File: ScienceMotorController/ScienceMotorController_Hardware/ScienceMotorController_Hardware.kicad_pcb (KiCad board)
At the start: 2 copper layers, 124.5 x 120.6 mm, 114 parts, among them SW1 SW_Push, SW2 SW_Push, SW3 SW_Push, SW4 SW_Push, SW5 SW_Push, U1 TM4C129E_Launchpad, U2 3.3V OKI, U4 VNH5019A_E, U5 VNH5019A_E, U6 VNH5019A_E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

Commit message: BOM
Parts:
- SW5: value SW_Push -> SW_SPDT; footprint Button_Switch_SMD:SW_SPST_TL3305A -> Button_Switch_THT:SW_CuK_OS102011MA1QN1_SPDT_Angled
- moved SW5 21.1 mm to (40.9, 116.1), turned to 270 degrees
- moved R56 16.5 mm to (45.5, 113.2), turned to 180 degrees
- moved SW3 5.59 mm to (49.7, 125.2)
- moved R31 5.59 mm to (41.5, 126.7)
- moved R32 5.59 mm to (59.8, 126.7)
- moved SW4 5.59 mm to (67.9, 125.2)
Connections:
- SW5 pad 1: +3V3 -> MSW_5
- SW5 pad 2: MSW_5 -> +3V3
- U1 pad PD3: MSW_5 -> MSW_4
- U1 pad PE0: MSW_1 -> MSW_5
- U1 pad PE1: MSW_2 -> MSW_1
- U1 pad PE3: MSW_4 -> MSW_2
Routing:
- net +3V3: track 473.8 -> 457.9 mm
- net MSW_5: track 19.8 -> 28.6 mm, vias 1 -> 0
- net MSW_4: track 38.8 -> 47.1 mm, vias 1 -> 3
- net MSW_3: track 23.9 -> 18.3 mm
- net MSW_2: track 53.4 -> 48.3 mm
- net MSW_1: track 38.0 -> 34.3 mm

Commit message: PRR Complete
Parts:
- added R34: 0, Resistor_SMD:R_0603_1608Metric_Pad1.05x0.95mm_HandSolder, F.Cu at (50.7, 96.8)
- added R57: 0, Resistor_SMD:R_0603_1608Metric_Pad1.05x0.95mm_HandSolder, F.Cu at (104.6, 96.8)
- added R58: 0, Resistor_SMD:R_0603_1608Metric_Pad1.05x0.95mm_HandSolder, F.Cu at (46.2, 96.8)
- added R59: 0, Resistor_SMD:R_0603_1608Metric_Pad1.05x0.95mm_HandSolder, F.Cu at (100.0, 96.8)
- added R60: 0, Resistor_SMD:R_0603_1608Metric_Pad1.05x0.95mm_HandSolder, F.Cu at (77.4, 96.6)
- added R61: 0, Resistor_SMD:R_0603_1608Metric_Pad1.05x0.95mm_HandSolder, F.Cu at (131.2, 97.1)
- added R62: 0, Resistor_SMD:R_0603_1608Metric_Pad1.05x0.95mm_HandSolder, F.Cu at (72.9, 96.6)
- added R63: 0, Resistor_SMD:R_0603_1608Metric_Pad1.05x0.95mm_HandSolder, F.Cu at (126.7, 97.1)
- D24, D25, D26, D27: value 3.3 -> 3.3 Zener
- D7: value SW_IND_4_LED -> SW_ERR_LED
- R29, R30, R31, R32, R56: value 500 -> 10k
- R36, R37, R38: value 500 -> 330
- R48, R49, R50, R51, R52, R53, R54, R55: value 1.5K -> 1K
- moved C10 88.9 mm to (66.0, 68.3), turned to 90 degrees
- moved C9 62.6 mm to (93.0, 68.3), turned to 90 degrees
- moved C3 27.6 mm to (119.9, 68.3), turned to 90 degrees
- moved C4 0.41 mm to (146.6, 68.3), turned to 90 degrees
- turned D24 to 90 degrees
- turned D25 to 90 degrees
- turned D26 to 90 degrees
- turned D27 to 90 degrees
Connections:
- D24 pad 1: GND -> M1_CS
- D24 pad 2: M1_CS -> GND
- D25 pad 1: GND -> M2_CS
- D25 pad 2: M2_CS -> GND
- D26 pad 1: GND -> M3_CS
- D26 pad 2: M3_CS -> GND
- D27 pad 1: GND -> M4_CS
- D27 pad 2: M4_CS -> GND
- U1 pad +5V': Net-(U1-Pad+5V') -> (no net)
- U1 pad Rese': Net-(U1-PadRese') -> (no net)
- U4 pad 6: GND -> Net-(R34-Pad2)
- U5 pad 6: GND -> Net-(R60-Pad2)
- U6 pad 6: GND -> Net-(R57-Pad2)
- U7 pad 6: GND -> Net-(R61-Pad2)
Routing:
- net Net-(R34-Pad2): track 0.00 -> 12.2 mm
- net Net-(R61-Pad2): track 0.00 -> 12.1 mm
- net Net-(R57-Pad2): track 0.00 -> 11.9 mm
- net Net-(R60-Pad2): track 0.00 -> 11.7 mm
- net +12VA: track 189.6 -> 199.3 mm
- net +3V3: track 457.9 -> 465.3 mm
- net GND: vias 26 -> 59
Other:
- board text added: "CCW"
- board text added: "CW"

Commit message: BOM Finished
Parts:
- D10: value LS_2_LED -> LS_4_LED
- D2: value LS_1_LED -> LS_3_LED
- R29, R30, R31, R32, R56: value 10k -> 10K
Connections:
- U1 pad +5V': (no net) -> Net-(U1-Pad+5V')
- U1 pad Rese': (no net) -> Net-(U1-PadRese')
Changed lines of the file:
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@@
     (zones 0)
     (modules 122)
-    (nets 164)
+    (nets 166)
   )
   (page A4)
@@
   )
   (setup
-    (last_trace_width 0.762)
+    (last_trace_width 0.25)
     (user_trace_width 0.254)
     (user_trace_width 0.381)
@@
   (net 162 "Net-(R60-Pad2)")
   (net 163 "Net-(R61-Pad2)")
+  (net 164 "Net-(U1-PadRese')")
+  (net 165 "Net-(U1-Pad+5V')")
   (net_class Default "This is the default net class."
     (clearance 0.2)
@@
     (add_net "Net-(R9-Pad2)")
     (add_net "Net-(SW5-Pad3)")
+    (add_net "Net-(U1-Pad+5V')")
     (add_net "Net-(U1-Pad+5V)")
     (add_net "Net-(U1-PadPA7)")
@@
     (add_net "Net-(U1-PadPQ0)")
     (add_net "Net-(U1-PadPQ2)")
+    (add_net "Net-(U1-PadRese')")
     (add_net "Net-(U1-PadRese)")
     (add_net "Net-(U4-Pad11)")
@@
       (effects (font (size 1 1) (thickness 0.15)))
     )
-    (fp_text value 10k (at 0 1.43) (layer F.Fab)
+    (fp_text value 10K (at 0 1.43) (layer F.Fab)
       (effects (font (size 1 1) (thickness 0.15)))
     )
@@
       (effects (font (size 1 1) (thickness 0.15)))
     )
-    (fp_text value 10k (at 0 1.43) (layer F.Fab)
+    (fp_text value 10K (at 0 1.43) (layer F.Fab)
       (effects (font (size 1 1) (thickness 0.15)))
     )
@@
       (effects (font (size 1 1) (thickness 0.15)))
     )
-    (fp_text value 10k (at 0 1.43) (layer F.Fab)
+    (fp_text value 10K (at 0 1.43) (layer F.Fab)
       (effects (font (size 1 1) (thickness 0.15)))
     )
@@
       (effects (font (size 1 1) (thickness 0.15)))
     )
-    (fp_text value 10k (at 0 1.43) (layer F.Fab)
+    (fp_text value 10K (at 0 1.43) (layer F.Fab)
       (effects (font (size 1 1) (thickness 0.15)))
     )
@@
       (effects (font (size 1 1) (thickness 0.15)))
     )
-    (fp_text value 10k (at 0 1.43 180) (layer F.Fab)
+    (fp_text value 10K (at 0 1.43 180) (layer F.Fab)
       (effects (font (size 1 1) (thickness 0.15)))
     )
@@
       (effects (font (size 1 1) (thickness 0.15)))
     )
-    (fp_text value LS_1_LED (at 0 1.43) (layer F.Fab)
+    (fp_text value LS_3_LED (at 0 1.43) (layer F.Fab)
       (effects (font (size 1 1) (thickness 0.15)))
     )
@@
       (effects (font (size 1 1) (thickness 0.15)))
     )
-    (fp_text value LS_2_LED (at 0 1.43) (layer F.Fab)
+    (fp_text value LS_4_LED (at 0 1.43) (layer F.Fab)
       (effects (font (size 1 1) (thickness 0.15)))
     )
@@
     (pad PA4 smd rect (at 85.09 -5.4864 180) (size 0.9906 1.778) (layers B.Cu B.Paste B.Mask)
       (net 80 SW_IND_2))
-    (pad Rese' smd rect (at 74.93 -48.6664 180) (size 0.9906 1.778) (layers B.Cu B.Paste B.Mask))
+    (pad Rese' smd rect (at 74.93 -48.6664 180) (size 0.9906 1.778) (layers B.Cu B.Paste B.Mask)
+      (net 164 "Net-(U1-PadRese')"))
     (pad PA7 smd rect (at 72.39 -48.6664 180) (size 0.9906 1.778) (layers B.Cu B.Paste B.Mask)
       (net 84 "Net-(U1-PadPA7)"))
@@
     (pad PK1 smd rect (at 77.47 -5.4864 180) (size 0.9906 1.778) (layers B.Cu B.Paste B.Mask)
       (net 86 "Net-(U1-PadPK1)"))
-    (pad +5V' smd rect (at 64.77 -5.4864 180) (size 0.9906 1.778) (layers B.Cu B.Paste B.Mask))
+    (pad +5V' smd rect (at 64.77 -5.4864 180) (size 0.9906 1.778) (layers B.Cu B.Paste B.Mask)
+      (net 165 "Net-(U1-Pad+5V')"))
     (pad GND smd rect (at 67.31 -5.4864 180) (size 0.9906 1.778) (layers B.Cu B.Paste B.Mask)
       (net 1 GND))
@@
   (gr_arc (start 163.068 152.146) (end 163.068 150.114) (angle -180) (layer Edge.Cuts) (width 0.15))
   (gr_arc (start 161.036 141.986) (end 163.068 141.986) (angle -90) (layer Edge.Cuts) (width 0.15))
-  (segment (start 76.508902 96.584504) (end 73.741901 96.584504) (width 0.254) (layer F.Cu) (net 162))
-  (segment (start 103.686902 96.838504) (end 100.919901 96.838504) (width 0.254) (layer F.Cu) (net 161))
-  (segment (start 130.356902 97.092504) (end 127.589901 97.092504) (width 0.254) (layer F.Cu) (net 163))
   (segment (start 54.356 101.459) (end 54.088 101.459) (width 0.254) (layer F.Cu) (net 1))
   (segment (start 54.088 101.459) (end 53.975 101.346) (width 0.254) (layer F.Cu) (net 1))
@@
   (segment (start 50.323999 93.679278) (end 49.33983 94.663447) (width 0.254) (layer F.Cu) (net 160))
   (segment (start 49.838902 96.838504) (end 47.071901 96.838504) (width 0.254) (layer F.Cu) (net 160))
+  (segment (start 103.686902 96.838504) (end 100.919901 96.838504) (width 0.254) (layer F.Cu) (net 161))
   (segment (start 103.686902 96.838504) (end 103.686902 93.163098) (width 0.254) (layer F.Cu) (net 161))
   (segment (start 104.386498 92.463502) (end 104.386498 87.9983) (width 0.254) (layer F.Cu) (net 161))
   (segment (start 103.686902 93.163098) (end 104.386498 92.463502) (width 0.254) (layer F.Cu) (net 161))
+  (segment (start 76.508902 96.584504) (end 73.741901 96.584504) (width 0.254) (layer F.Cu) (net 162))
   (segment (start 77.335498 87.9983) (end 77.335498 93.860502) (width 0.254) (layer F.Cu) (net 162))
   (segment (start 76.508902 94.687098) (end 77.335498 93.860502) (width 0.254) (layer F.Cu) (net 162))
   (segment (start 76.508902 96.584504) (end 76.508902 94.687098) (width 0.254) (layer F.Cu) (net 162))
+  (segment (start 130.356902 97.092504) (end 127.589901 97.092504) (width 0.254) (layer F.Cu) (net 163))
   (segment (start 131.056498 93.987502) (end 131.056498 88.001296) (width 0.254) (layer F.Cu) (net 163))
   (segment (start 130.356902 97.092504) (end 130.356902 94.687098) (width 0.254) (layer F.Cu) (net 163))

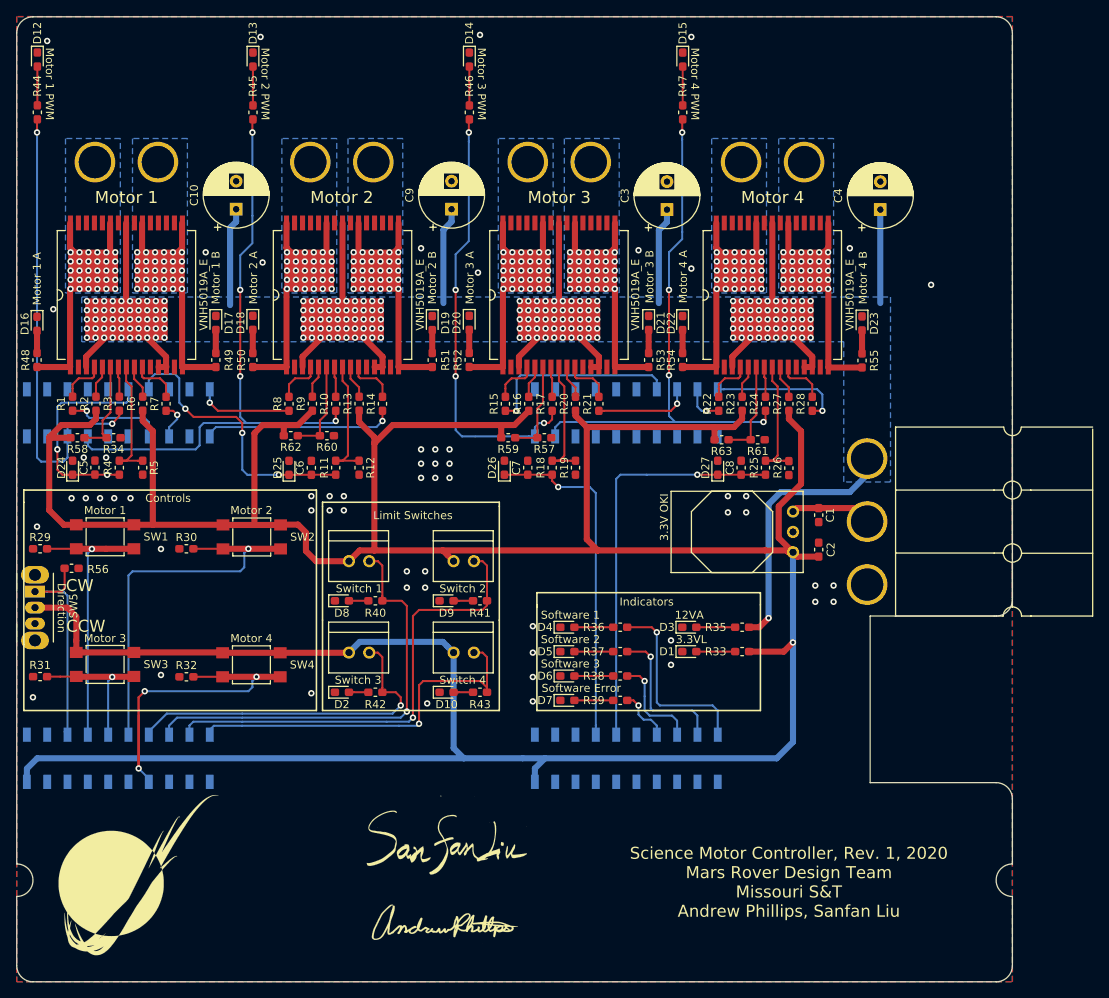
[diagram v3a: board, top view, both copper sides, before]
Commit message: Step files, updated pin layout, cleaned schematic
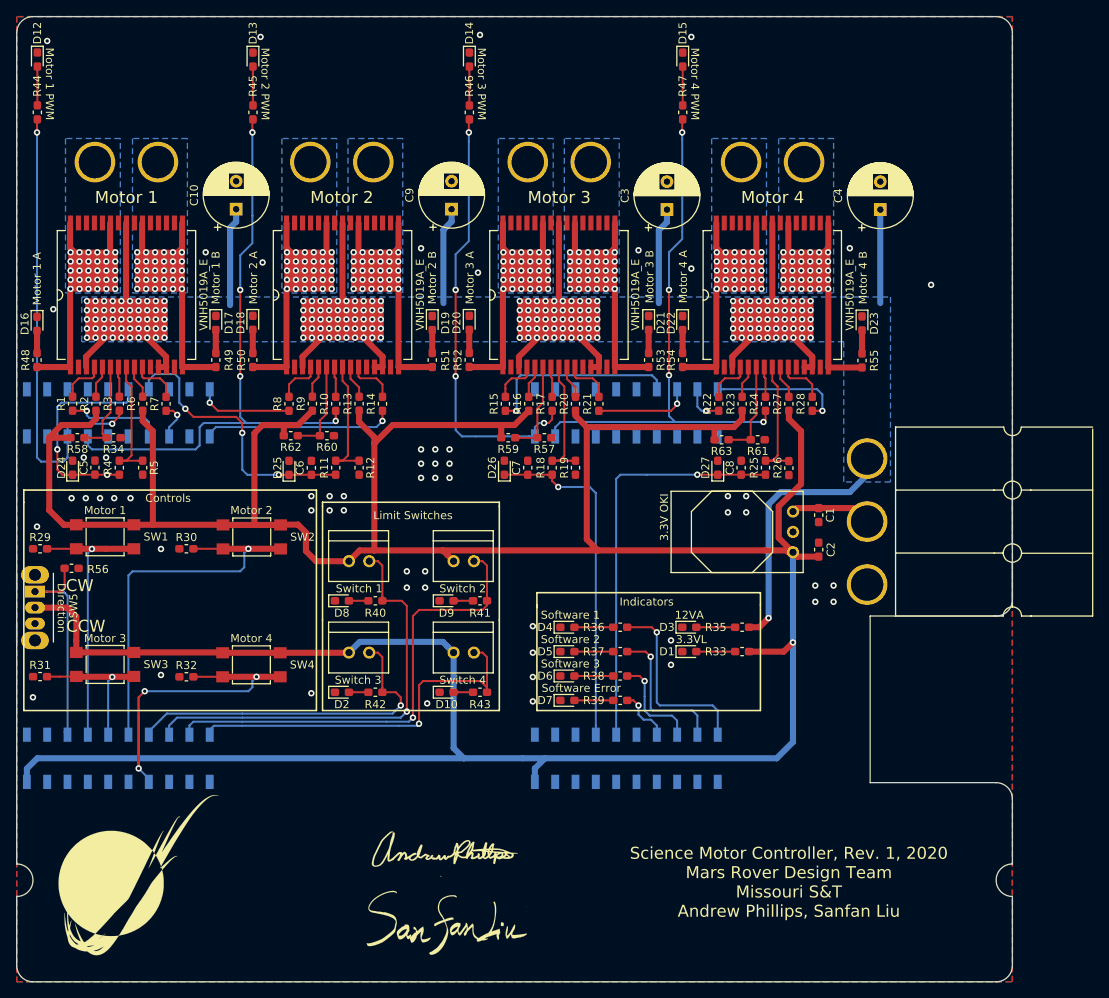
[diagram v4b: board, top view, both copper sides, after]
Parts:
- moved G*** 10.0 mm to (92.1, 157.5)
- moved G*** 9.14 mm to (91.9, 148.6)
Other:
- board size 124.5 x 120.6 mm -> 124.5 x 120.7 mm
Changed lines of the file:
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@@
   (general
     (thickness 1.6)
-    (drawings 80)
+    (drawings 76)
     (tracks 1222)
     (zones 0)
@@
     (42 Eco1.User user)
     (43 Eco2.User user)
-    (44 Edge.Cuts user hide)
+    (44 Edge.Cuts user)
     (45 Margin user)
     (46 B.CrtYd user)
@@
   )
   (module MRDT_Silkscreens:z_sig_SanfanLiu_sig21.8mmx12.3mm1 (layer F.Cu)
-    (at 92.075 147.447)
+    (at 92.075 157.48)
     (fp_text reference G*** (at 13.462 0) (layer F.SilkS) hide
       (effects (font (size 1.524 1.524) (thickness 0.3)))
@@
   )
   (module MRDT_Silkscreens:z_sig_Andrew_Phillips_Sig_19.7mmx7.7mm (layer F.Cu)
-    (at 91.948 157.734)
+    (at 91.948 148.59)
     (fp_text reference G*** (at 13.589 0) (layer F.SilkS) hide
       (effects (font (size 1.524 1.524) (thickness 0.3)))
@@
     )
   )
+  (gr_line (start 38.608 46.228) (end 38.608 150.114) (layer Edge.Cuts) (width 0.15))
+  (gr_line (start 163.068 46.228) (end 163.068 117.094) (layer Edge.Cuts) (width 0.15))
+  (gr_line (start 40.64 44.196) (end 161.036 44.196) (layer Edge.Cuts) (width 0.15))
+  (gr_arc (start 40.64 46.228) (end 40.64 44.196) (angle -90) (layer Edge.Cuts) (width 0.15))
+  (gr_arc (start 161.036 46.228) (end 163.068 46.228) (angle -90) (layer Edge.Cuts) (width 0.15))
   (gr_text CCW (at 47.244 120.396) (layer F.SilkS)
     (effects (font (size 1.5 1.5) (thickness 0.3)))
@@
   (gr_line (start 131.572 130.937) (end 103.632 130.937) (layer F.SilkS) (width 0.2))
   (gr_line (start 131.572 116.205) (end 103.632 116.205) (layer F.SilkS) (width 0.2))
-  (gr_line (start 163.068 61.976) (end 163.068 46.228) (layer Edge.Cuts) (width 0.15))
-  (gr_line (start 38.608 61.976) (end 38.608 46.228) (layer Edge.Cuts) (width 0.15))
   (gr_line (start 76.073 130.937) (end 76.073 103.378) (layer F.SilkS) (width 0.2))
   (gr_line (start 39.497 122.682) (end 39.497 130.937) (layer F.SilkS) (width 0.2))
@@
     (effects (font (size 1 1) (thickness 0.15)))
   )
-  (gr_line (start 163.068 83.566) (end 163.068 61.976) (layer Edge.Cuts) (width 0.15))
-  (gr_line (start 38.608 61.976) (end 38.608 83.566) (layer Edge.Cuts) (width 0.15))
-  (gr_arc (start 40.64 46.2534) (end 40.64 44.2214) (angle -90) (layer Edge.Cuts) (width 0.15))
-  (gr_arc (start 161.036 46.2534) (end 163.068 46.2534) (angle -90) (layer Edge.Cuts) (width 0.15))
-  (gr_line (start 161.036 44.2214) (end 40.64 44.2214) (layer Edge.Cuts) (width 0.15))
-  (gr_line (start 38.608 150.114) (end 38.608 83.566) (layer Edge.Cuts) (width 0.15))
-  (gr_line (start 163.068 117.094) (end 163.068 83.566) (layer Edge.Cuts) (width 0.15))
   (gr_line (start 145.288 119.126) (end 161.036 119.126) (layer Edge.Cuts) (width 0.15))
   (gr_line (start 145.288 139.954) (end 145.288 119.126) (layer Edge.Cuts) (width 0.15))
